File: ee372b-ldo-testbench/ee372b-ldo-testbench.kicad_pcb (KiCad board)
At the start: 2 copper layers, 123 parts, among them J1 PEC02SAAN, J10 OUT_S, J11 VOUT, J12 VDD_BUF, J13 V_SIG, J14 PEC03SAAN, J15 VSIG_BUF, J16 PEC03SAAN, J17 PEC03SAAN, J18 PEC03SAAN, J19 PEC03SAAN, J2 PEC02SAAN, J20 VREF_EXTERNAL, J21 PEC02SAAN, J22 PEC02SAAN, J23 PEC02SAAN, J3 GND, J4 1V8, J5 VOUT, J6 GND, J7 PEC02SAAN, J8 VIN, J9 IN_S, Q1 FDV305N, Q2 FDV305N, Q3 FDV305N, Q4 FDV305N, Q5 FDV305N, U1 MMSZ4679T1G, U3 ADS1220IPW, U4 BUF634AIDR

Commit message: updated pcb layout settings to 4 layers
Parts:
- added R63: 0, Resistor_SMD:R_0805_2012Metric_Pad1.20x1.40mm_HandSolder, F.Cu at (97.5, 114.5)
- added TP8: VARIABLE_LOAD_VOUT, 1_EE372_DemoBoard:KEYSTONE_5016, F.Cu at (108.0, 127.5)
- added TP9: VARIABLE_LOAD_GND, 1_EE372_DemoBoard:KEYSTONE_5016, F.Cu at (108.0, 132.5)
- moved A1 217.0 mm to (272.9, -48.4)
- moved J11 155.0 mm to (-29.0, 36.1)
- moved R10 154.3 mm to (95.0, 139.0), turned to -90 degrees
- moved J14 146.2 mm to (99.5, 142.5), turned to 90 degrees
- moved R12 145.3 mm to (86.5, 139.0), turned to -90 degrees
- moved R15 143.5 mm to (70.0, 139.0), turned to -90 degrees
- moved R11 138.0 mm to (97.5, 122.0), turned to -90 degrees
- moved J16 137.2 mm to (90.5, 142.5), turned to 90 degrees
- moved R14 136.5 mm to (78.0, 139.0), turned to -90 degrees
- moved R17 135.7 mm to (61.5, 139.0), turned to -90 degrees
- moved J17 128.7 mm to (82.0, 142.5), turned to 90 degrees
- moved R16 128.5 mm to (81.5, 122.0), turned to -90 degrees
- moved R13 128.4 mm to (88.5, 122.0), turned to -90 degrees
- moved R20 123.9 mm to (62.0, 122.0), turned to -90 degrees
- moved R18 121.1 mm to (76.5, 122.0), turned to -90 degrees
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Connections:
- R11 pad 1: /VOUT -> /VARIABLE_LOAD
- R13 pad 1: /VOUT -> /VARIABLE_LOAD
- R16 pad 1: /VOUT -> /VARIABLE_LOAD
- R18 pad 1: /VOUT -> /VARIABLE_LOAD
- R19 pad 1: /VOUT -> /VARIABLE_LOAD
- R20 pad 1: /VOUT -> /VARIABLE_LOAD
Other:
- copper layers 2 -> 4

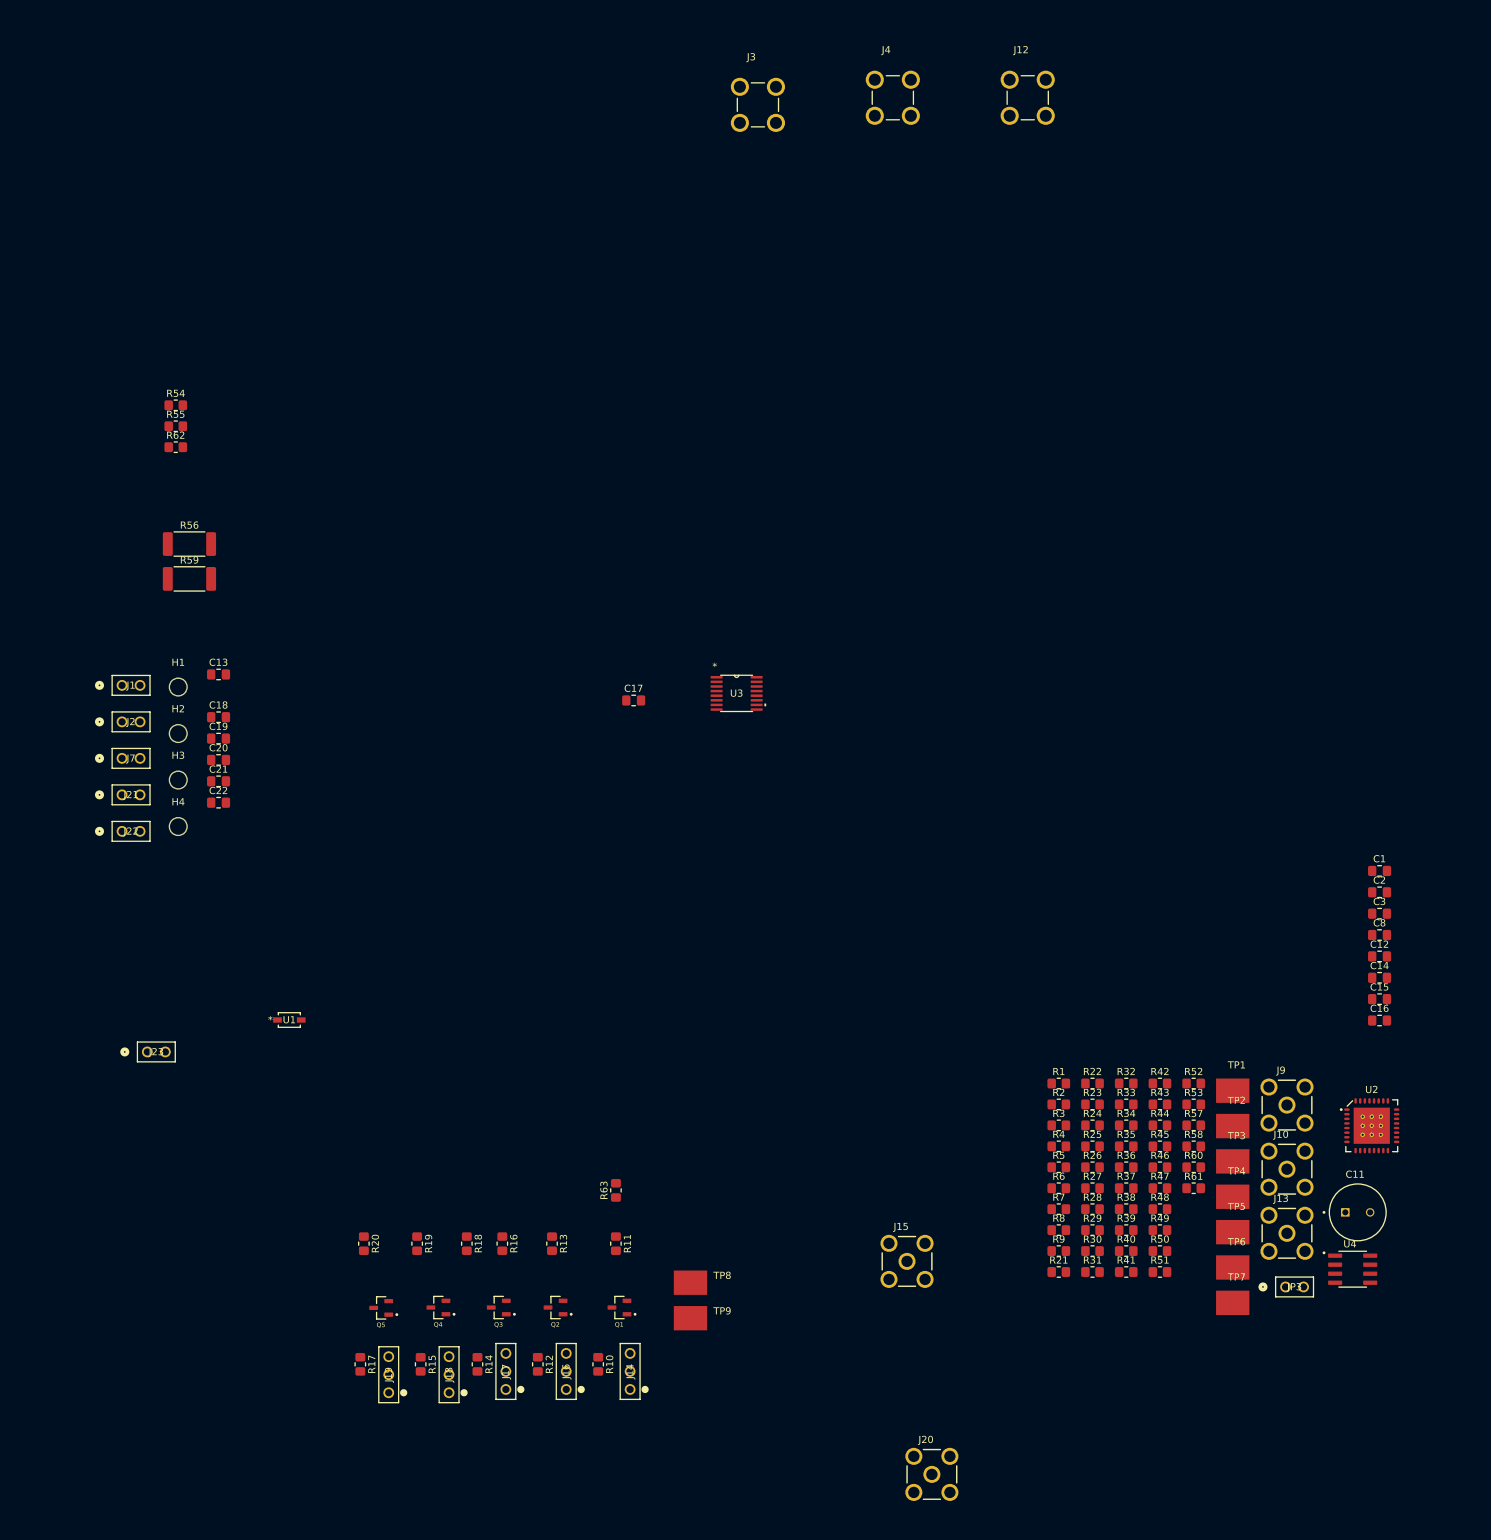
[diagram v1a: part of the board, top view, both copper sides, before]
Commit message: tweaks to schematic, more bypass caps, ext 3v3 source
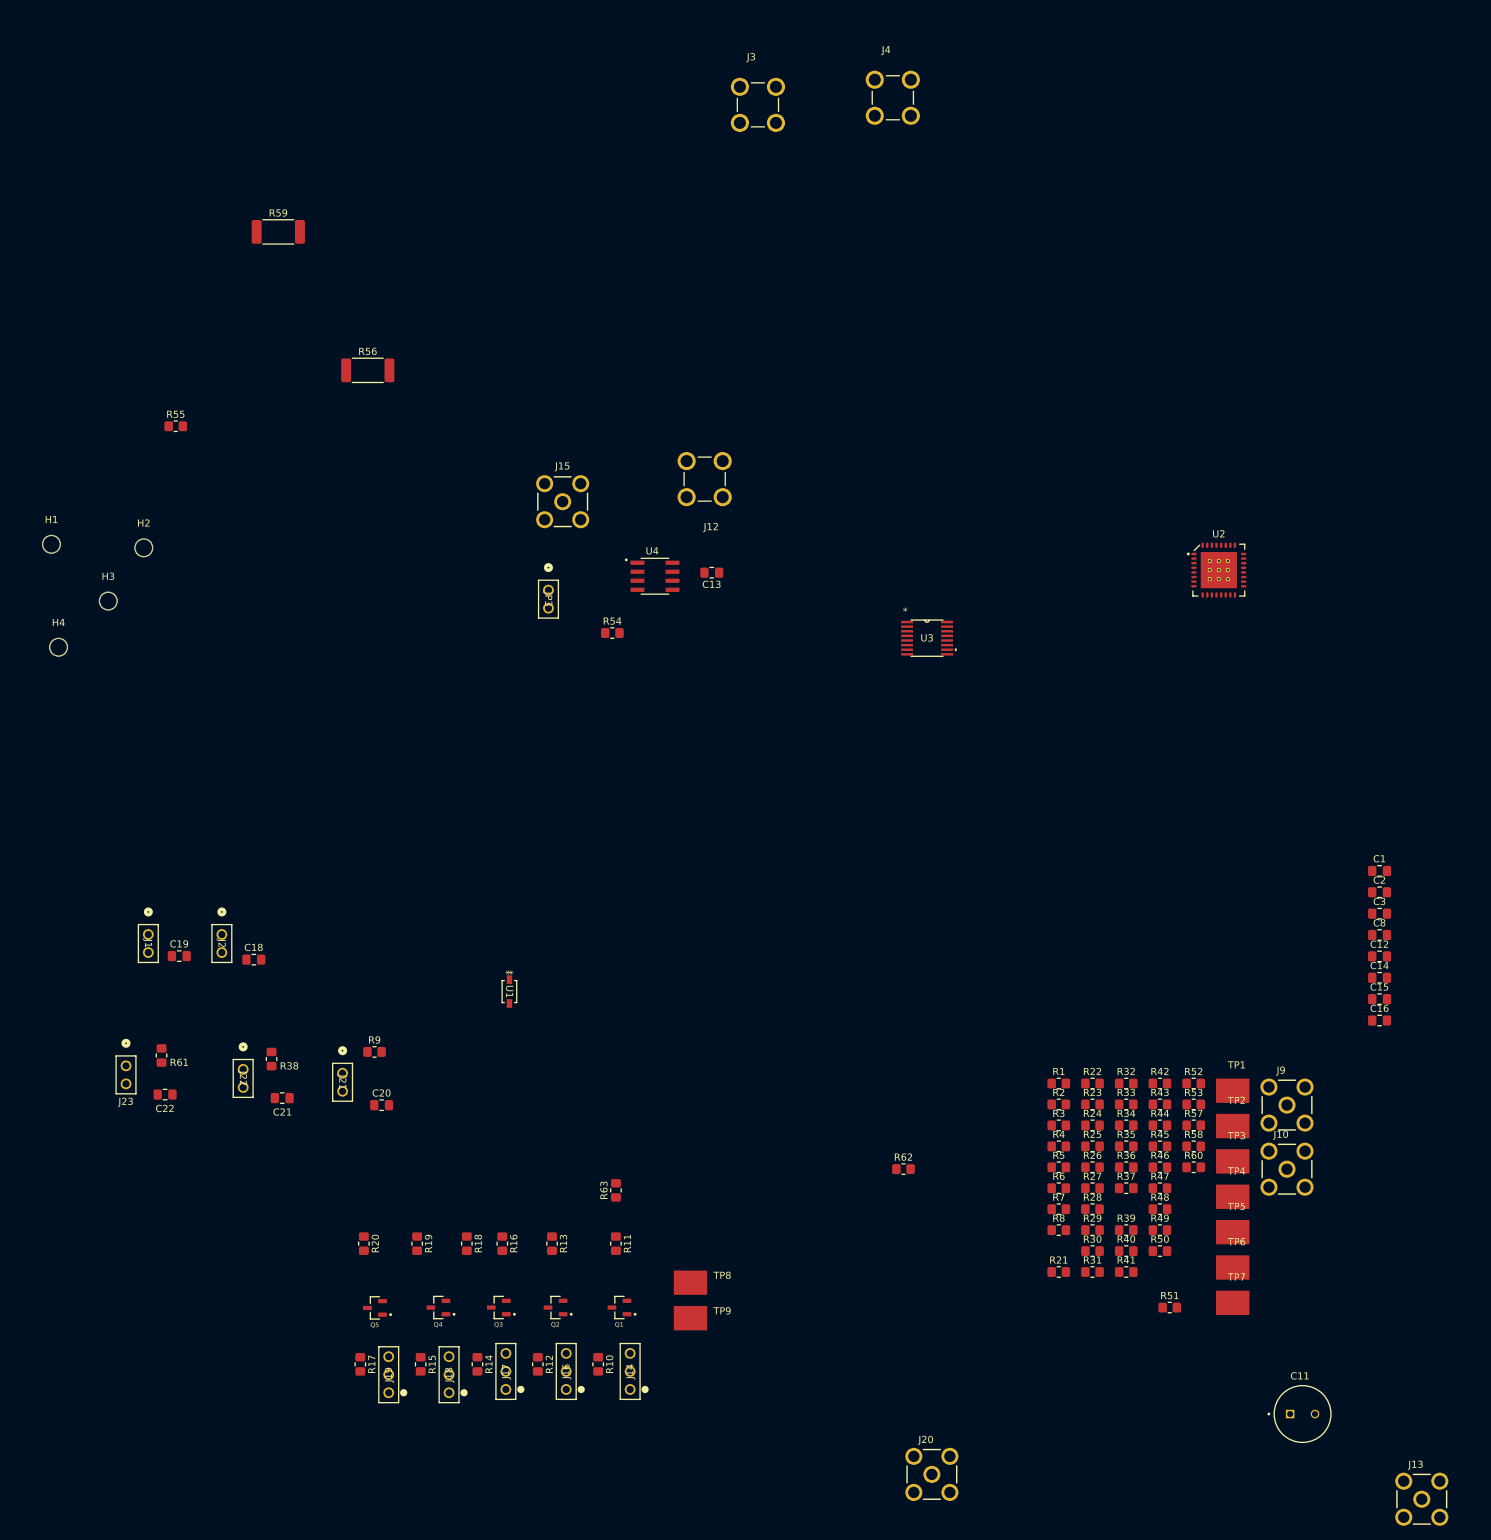
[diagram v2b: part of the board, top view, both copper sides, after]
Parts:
- removed C17: 10uF, Capacitor_SMD:C_0805_2012Metric_Pad1.18x1.45mm_HandSolder
- removed J7: PEC02SAAN, 1_EE372_DemoBoard:CONN_PxC02S_SUL
- C18: value 100nF -> 1uF
- C19: value 0.1nF -> 10nF
- moved R61 146.6 mm to (33.5, 95.5), turned to 90 degrees
- moved R62 144.4 mm to (138.0, 111.5)
- moved JP3 142.9 mm to (88.0, 30.0), turned to -90 degrees
- moved U4 138.5 mm to (103.0, 28.0)
- moved R38 122.2 mm to (49.0, 96.0), turned to -90 degrees
- moved J15 117.5 mm to (90.0, 17.5)
- moved R9 100.4 mm to (63.5, 95.0)
- moved U2 81.2 mm to (182.4, 27.1)
- moved C13 70.9 mm to (111.0, 27.5), turned to 180 degrees
- moved J12 70.4 mm to (110.0, 14.3), turned to 180 degrees
- moved R54 69.4 mm to (97.0, 36.0)
- moved C20 53.8 mm to (64.5, 102.5)
- moved R59 50.5 mm to (50.0, -20.5)
- moved J21 50.0 mm to (59.0, 98.0), turned to -90 degrees
- moved C21 45.5 mm to (50.5, 101.5)
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
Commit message: tried to group things together
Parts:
- removed J6: GND, 1_EE372_DemoBoard:CALTEST_CT3151-2
- removed R45, R46, R47: 0, Resistor_SMD:R_0805_2012Metric_Pad1.20x1.40mm_HandSolder
- added C10: 100nF, Capacitor_SMD:C_0805_2012Metric_Pad1.18x1.45mm_HandSolder, F.Cu at (576.3, 155.0)
- added C17: 100nF, Capacitor_SMD:C_0805_2012Metric_Pad1.18x1.45mm_HandSolder, F.Cu at (576.3, 158.0)
- added C23: 100nF, Capacitor_SMD:C_0805_2012Metric_Pad1.18x1.45mm_HandSolder, F.Cu at (576.3, 161.0)
- added C24: 100nF, Capacitor_SMD:C_0805_2012Metric_Pad1.18x1.45mm_HandSolder, F.Cu at (581.2, 152.0)
- added C25: 1uF, Capacitor_SMD:C_0805_2012Metric_Pad1.18x1.45mm_HandSolder, F.Cu at (72.5, 102.0)
- added C26: 10uF, Capacitor_SMD:C_0805_2012Metric_Pad1.18x1.45mm_HandSolder, F.Cu at (368.5, 148.0)
- added C27: 1uF, Capacitor_SMD:C_0805_2012Metric_Pad1.18x1.45mm_HandSolder, F.Cu at (581.2, 158.0)
- added C28: 10uF, Capacitor_SMD:C_0805_2012Metric_Pad1.18x1.45mm_HandSolder, F.Cu at (368.5, 154.0)
- added C4: 100nF, Capacitor_SMD:C_0805_2012Metric_Pad1.18x1.45mm_HandSolder, F.Cu at (571.5, 152.0)
- added C5: 100nF, Capacitor_SMD:C_0805_2012Metric_Pad1.18x1.45mm_HandSolder, F.Cu at (571.5, 155.0)
- added C6: 100nF, Capacitor_SMD:C_0805_2012Metric_Pad1.18x1.45mm_HandSolder, F.Cu at (571.5, 158.0)
- added C7: 100nF, Capacitor_SMD:C_0805_2012Metric_Pad1.18x1.45mm_HandSolder, F.Cu at (571.5, 161.0)
- added C9: 100nF, Capacitor_SMD:C_0805_2012Metric_Pad1.18x1.45mm_HandSolder, F.Cu at (576.3, 152.0)
- added J24: PEC02SAAN, 1_EE372_DemoBoard:CONN_PxC02S_SUL, F.Cu at (68.0, 98.0)
- added J25: PEC03SAAN, 1_EE372_DemoBoard:CONN_PEC03SAAN_SUL, F.Cu at (221.5, 90.5)
- added TP10: 1V8, 1_EE372_DemoBoard:KEYSTONE_5016, F.Cu at (253.4, 317.5)
- C20: value 0.1nF -> 1nF
- J5: value VOUT -> 3v3_EXTERNAL
- moved J11 524.0 mm to (466.0, -135.9)
- moved R59 455.6 mm to (496.5, -111.0)
- moved J13 424.1 mm to (-44.5, -180.5)
- moved J8 396.5 mm to (269.5, -255.4)
- moved J20 384.6 mm to (522.0, 213.5)
- moved J9 378.8 mm to (238.0, -273.5)
- moved C11 378.8 mm to (240.2, -230.0)
- moved TP1 378.8 mm to (230.3, -275.6)
- moved TP2 378.8 mm to (230.3, -270.6)
- moved R21 370.3 mm to (524.0, 193.5)
- moved R22 370.3 mm to (528.8, 166.9)
- moved R23 370.3 mm to (528.8, 169.9)
- moved R24 370.3 mm to (528.8, 172.8)
- moved R25 370.3 mm to (528.8, 175.8)
- moved R26 370.3 mm to (528.8, 178.7)
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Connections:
- A1 pad 36: /3V3 -> /3V3_PICO
- C3 pad 2: /3V3 -> /3V3_PICO
- J1 pad 1: /1V8 -> /c1_vin_jump
- J2 pad 1: /1V8 -> /c1_vin_jump
- J4 pad 1: GND -> Net-(J4-Pin_1)
- J5 pad 1: /VOUT -> Net-(J5-Pin_1)
- R39 pad 1: Net-(R39-Pad1) -> GND
- R39 pad 2: /1V8 -> Net-(C21-Pad1)
- R40 pad 1: Net-(R40-Pad1) -> GND
- R40 pad 2: /1V8 -> Net-(C22-Pad1)
- R41 pad 1: Net-(R41-Pad1) -> GND
- R41 pad 2: /1V8 -> Net-(C20-Pad1)
- R42 pad 1: Net-(R42-Pad1) -> /LDO_VOUT
- R42 pad 2: /1V8 -> Net-(J24-Pad1)
- R43 pad 1: Net-(R43-Pad1) -> GND
- R43 pad 2: /1V8 -> Net-(C25-Pad1)
- R44 pad 1: Net-(R44-Pad1) -> Net-(J25-Pad3)
- R44 pad 2: /1V8 -> /3V3_PICO
- R56 pad 2: /1V8 -> /c1_vin_jump
- TP2 pad 1: /1V8 -> /c1_vin_jump
- TP7 pad 1: GND -> Net-(J4-Pin_1)
- U2 pad 14: Net-(R41-Pad1) -> Net-(C6-Pad2)
- U2 pad 16: Net-(R42-Pad1) -> Net-(C7-Pad2)
- U2 pad 17: Net-(R43-Pad1) -> Net-(C9-Pad2)
- U2 pad 2: Net-(R39-Pad1) -> /c1_vin_jump
- U2 pad 21: Net-(R44-Pad1) -> Net-(C10-Pad2)
- U2 pad 8: Net-(R40-Pad1) -> Net-(C5-Pad2)

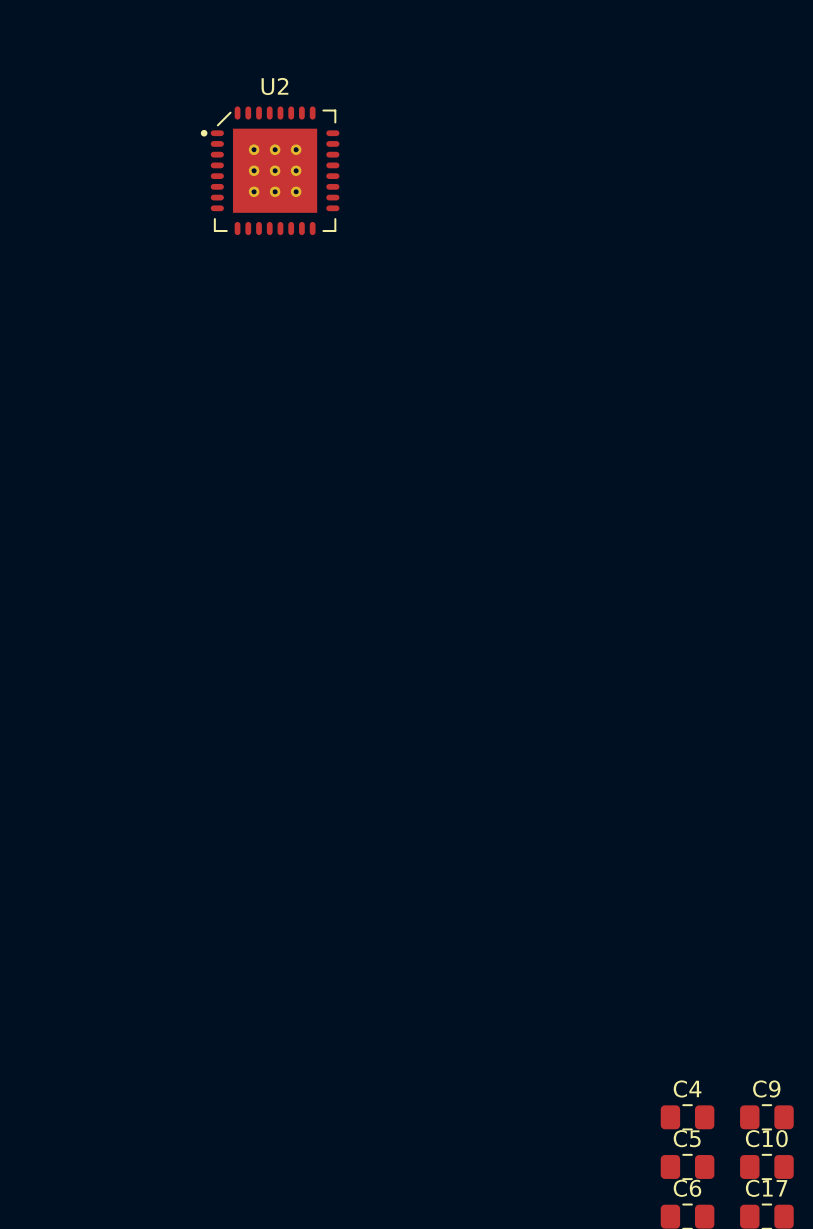
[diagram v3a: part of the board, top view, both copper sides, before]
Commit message: updated QFN courtyard
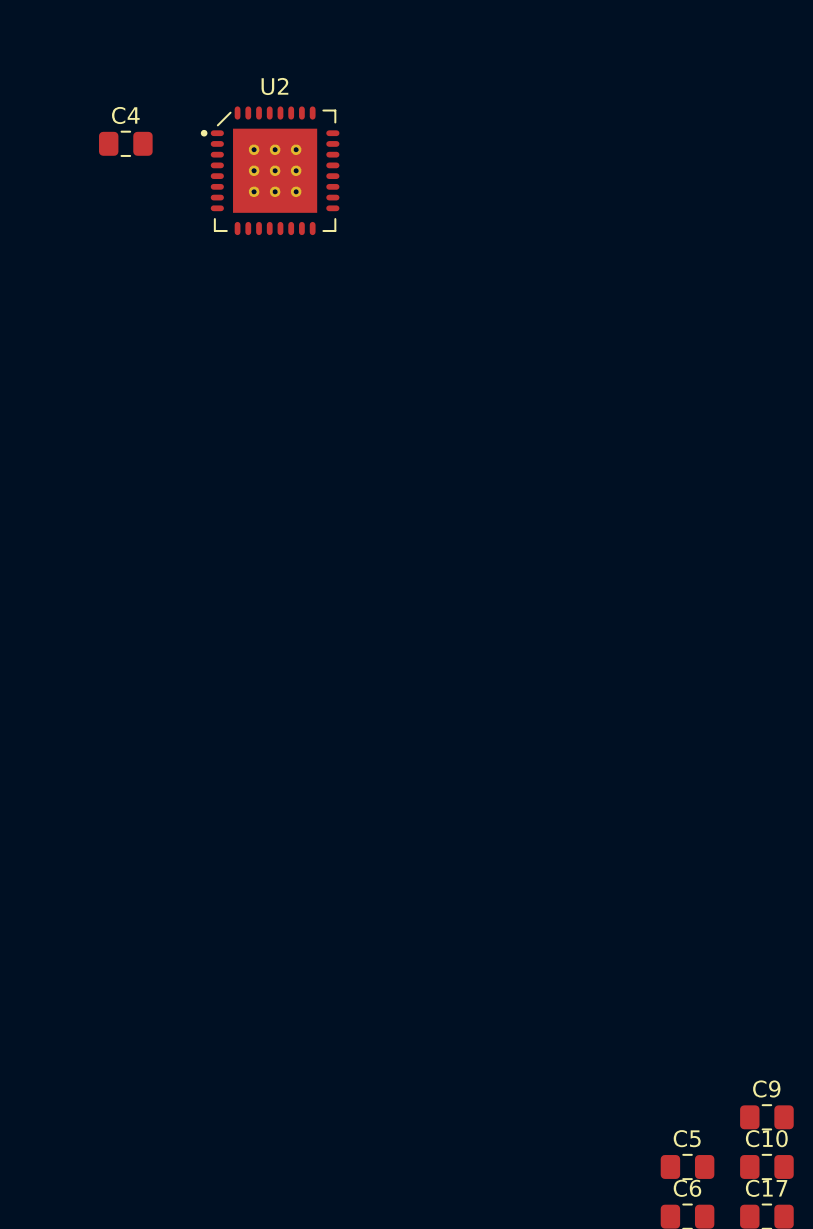
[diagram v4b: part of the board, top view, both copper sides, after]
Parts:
- moved C4 68.1 mm to (537.5, 93.0)
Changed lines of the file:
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@@
 		(sheetname "/")
 		(sheetfile "ee372b-ldo-testbench.kicad_sch")
-		(units
-			(unit
-				(name "A")
-				(pins "19" "1" "3" "33" "4" "6" "2" "7" "8" "13" "14" "18" "16" "20"
-					"17" "22" "21" "23" "24" "25" "27" "26" "32" "28" "29" "30" "31" "5"
-					"15" "9" "10" "11" "12"
-				)
-			)
-		)
 		(attr smd)
 		(duplicate_pad_numbers_are_jumpers no)
@@
 		)
 		(fp_line
-			(start -6.9 -6.9)
-			(end 6.9 -6.9)
+			(start -3.944455 -3.944455)
+			(end 3.944455 -3.944455)
 			(stroke
-				(width 0.05)
+				(width 0.028583)
 				(type default)
 			)
@@
 		)
 		(fp_line
-			(start -6.9 6.9)
-			(end -6.9 -6.9)
+			(start -3.944455 3.944455)
+			(end -3.944455 -3.944455)
 			(stroke
-				(width 0.05)
+				(width 0.028583)
 				(type default)
 			)
@@
 		)
 		(fp_line
-			(start 6.9 -6.9)
-			(end 6.9 6.9)
+			(start 3.944455 -3.944455)
+			(end 3.944455 3.944455)
 			(stroke
-				(width 0.05)
+				(width 0.028583)
 				(type default)
 			)
@@
 		)
 		(fp_line
-			(start 6.9 6.9)
-			(end -6.9 6.9)
+			(start 3.944455 3.944455)
+			(end -3.944455 3.944455)
 			(stroke
-				(width 0.05)
+				(width 0.028583)
 				(type default)
 			)
@@
 	(footprint "Capacitor_SMD:C_0805_2012Metric_Pad1.18x1.45mm_HandSolder"
 		(layer "F.Cu")
-		(at 571.5375 151.99)
+		(at 537.5 93)
 		(descr "Capacitor SMD 0805 (2012 Metric), square (rectangular) end terminal, IPC-7351 nominal with elongated pad for handsoldering. (Body size source: IPC-SM-782 page 76, https://www.pcb-3d.com/wordpress/wp-content/uploads/ipc-sm-782a_amendment_1_and_2.pdf, https://docs.google.com/spreadsheets/d/1BsfQQcO9C6DZCsRaXUlFlo91Tg2WpOkGARC1WS5S8t0/edit?usp=sharing)")
 		(tags "capacitor handsolder")
